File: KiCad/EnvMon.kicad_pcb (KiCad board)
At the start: 2 copper layers, 44.5 x 37 mm, 22 parts, among them J1 USB-C, J2 DC, J3 GPIO, M2 OLED1.5-RGB, M3 SCD30-4pin, U1 FT231XQ, U2 ESP32-WROOM-32

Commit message: Tidy
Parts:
- removed the R10 at (132.0, 91.5)
- added R3: 732R, RevK:R_0603, F.Cu at (99.2, 68.9)
- added R4: 2K, RevK:R_0603, F.Cu at (99.2, 66.5)
- added R5: 324R, RevK:R_0603, F.Cu at (99.2, 67.7)
- D1: value LED -> RGB; footprint LED_SMD:LED_0603_1608Metric -> RevK:LED-RGB-1.6x1.6
- J3: footprint Connector_Molex:Molex_SPOX_5268-08A_1x08_P2.50mm_Horizontal -> RevK:Molex_MiniSPOX_H8RA
- moved D1 43.3 mm to (99.2, 64.7), turned to 180 degrees
- moved J3 8.75 mm to (117.8, 93.2)
- renumbered Logo3 to Logo1, Logo1 to Logo2, Logo2 to Logo3, M3 to M1, R7 to R10, R8 to R11, R9 to R12, R3 to R6, R4 to R7, R5 to R8, R6 to R9
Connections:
- D1 pad 1: Net-(D1-Pad1) -> +3V3
- U2 pad 14: Net-(U2-Pad14) -> R
- U2 pad 23: Net-(U2-Pad23) -> B
- U2 pad 24: Net-(D1-Pad1) -> G
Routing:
- net GND: track 75.8 -> 145.3 mm, vias 1 -> 2
- net G: track 0.00 -> 46.6 mm, vias 0 -> 2
- net B: track 0.00 -> 43.8 mm, vias 0 -> 2
- net R: track 0.00 -> 40.0 mm, vias 0 -> 4
- net Net-(D1-Pad1): track 14.8 -> 0.00 mm, vias 2 -> 0
- net +3V3: track 104.9 -> 97.5 mm, vias 5 -> 4
- net Net-(U1-Pad1): track 48.1 -> 52.8 mm
- net Net-(D1-Pad2): track 1.52 -> 5.97 mm
- net Net-(D1-Pad4): track 0.00 -> 3.44 mm
- net IO4: track 25.8 -> 28.7 mm
- net IO3: track 33.2 -> 30.6 mm
- net Net-(U1-Pad18): track 30.3 -> 32.7 mm
- net IO1: track 21.9 -> 20.0 mm
- net Net-(U1-Pad19): track 55.9 -> 54.5 mm
- net IO2: track 20.4 -> 21.8 mm
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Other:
- board text added: "2021-07-20"
- board text removed: "2021-06-17"

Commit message: Move resistors
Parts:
- R1, R2: moved to F.Cu
- moved R1 8.76 mm to (93.3, 92.5)
- moved R2 7.91 mm to (91.8, 92.5)
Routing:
- net GND: track 145.3 -> 160.4 mm, vias 2 -> 3
- net Net-(J1-PadB5): track 9.14 -> 13.3 mm, vias 1 -> 2
- net Net-(J1-PadA5): track 11.8 -> 9.69 mm, vias 1 -> 2
- net IO6: track 29.2 -> 30.2 mm
- net Net-(J1-PadA7): track 7.92 -> 8.90 mm
- net Net-(J1-PadA6): track 8.06 -> 8.99 mm
- net Net-(J1-PadA4): track 31.8 -> 30.9 mm

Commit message: Library update
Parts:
- removed Reg1: Regulator, RevK:RegulatorBlock
- added C1: 0.1uF, RevK:Hidden, F.Cu at (95.3, 78.5)
- added C2: 2.2uF, RevK:Hidden, F.Cu at (96.5, 82.0)
- added C3: 10uF, RevK:Hidden, F.Cu at (102.8, 82.0)
- added D1: Schottky, RevK:Hidden, F.Cu at (99.7, 81.7)
- added L1: 6.8uH, RevK:Hidden, F.Cu at (101.3, 78.5)
- added U1: LMR16006YQ3, RevK:RegulatorBlock, F.Cu at (97.4, 78.5)
- renumbered D1 to D2, U1 to U2, U2 to U3

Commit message: Kicad 6
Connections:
- J1 pad A8: Net-(J1-PadA8) -> unconnected-(J1-PadA8)
- J1 pad B8: Net-(J1-PadB8) -> unconnected-(J1-PadB8)
- U2 pad 14: Net-(U2-Pad14) -> unconnected-(U2-Pad14)
- U2 pad 15: Net-(U2-Pad15) -> unconnected-(U2-Pad15)
- U2 pad 16: Net-(U2-Pad16) -> unconnected-(U2-Pad16)
- U2 pad 7: Net-(U2-Pad7) -> unconnected-(U2-Pad7)
- U3 pad 17: Net-(U3-Pad17) -> unconnected-(U3-Pad17)
- U3 pad 18: Net-(U3-Pad18) -> unconnected-(U3-Pad18)
- U3 pad 19: Net-(U3-Pad19) -> unconnected-(U3-Pad19)
- U3 pad 20: Net-(U3-Pad20) -> unconnected-(U3-Pad20)
- U3 pad 21: Net-(U3-Pad21) -> unconnected-(U3-Pad21)
- U3 pad 22: Net-(U3-Pad22) -> unconnected-(U3-Pad22)
- U3 pad 32: Net-(U3-Pad32) -> unconnected-(U3-Pad32)
- U3 pad 4: Net-(U3-Pad4) -> unconnected-(U3-Pad4)
- U3 pad 5: Net-(U3-Pad5) -> unconnected-(U3-Pad5)
- U3 pad 6: Net-(U3-Pad6) -> unconnected-(U3-Pad6)
- U3 pad 7: Net-(U3-Pad7) -> unconnected-(U3-Pad7)
- U3 pad 8: Net-(U3-Pad8) -> unconnected-(U3-Pad8)
- U3 pad 9: Net-(U3-Pad9) -> unconnected-(U3-Pad9)
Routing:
- net IO4: track 28.7 -> 27.8 mm
- net GND: track 160.4 -> 159.6 mm
- net OLED-MOSI: track 36.9 -> 36.1 mm
- net Net-(U2-Pad18): track 32.7 -> 32.1 mm
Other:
- net class Default removed

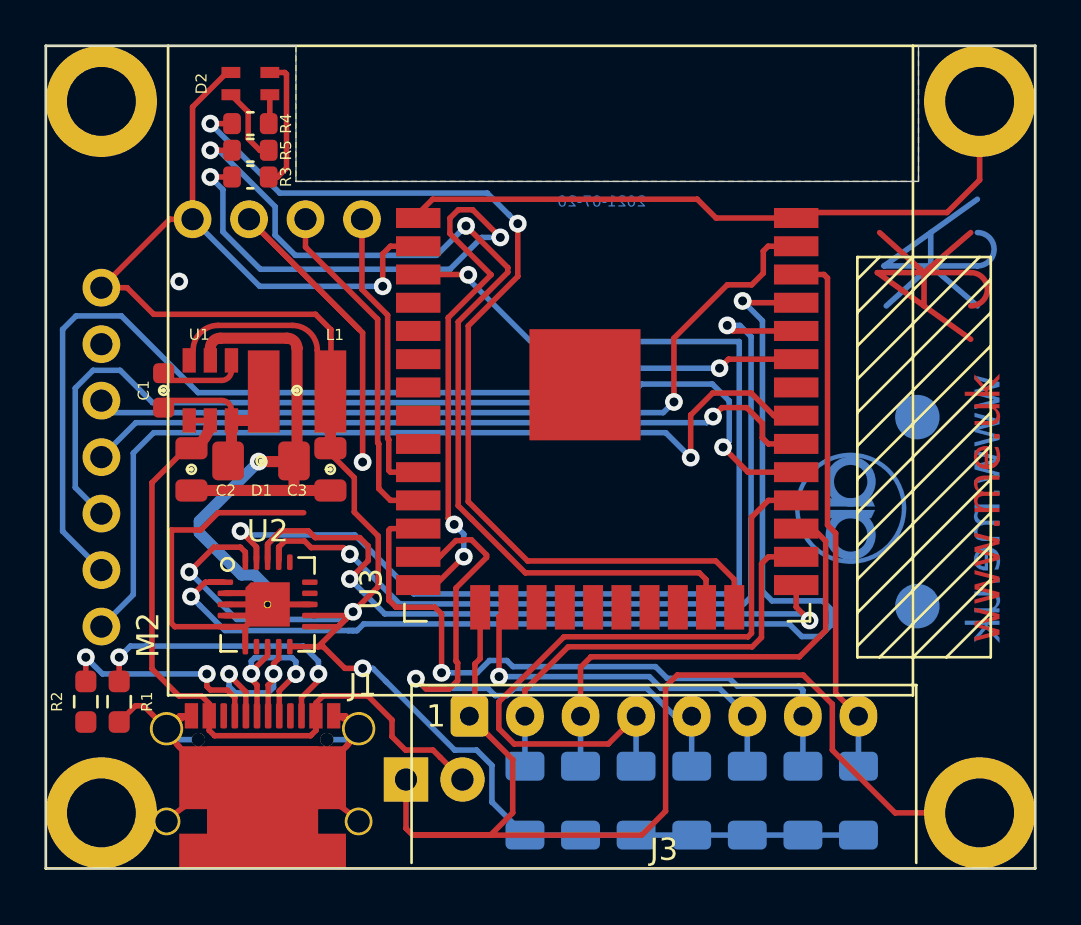
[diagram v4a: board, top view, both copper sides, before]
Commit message: More KiCad 6 tweaks
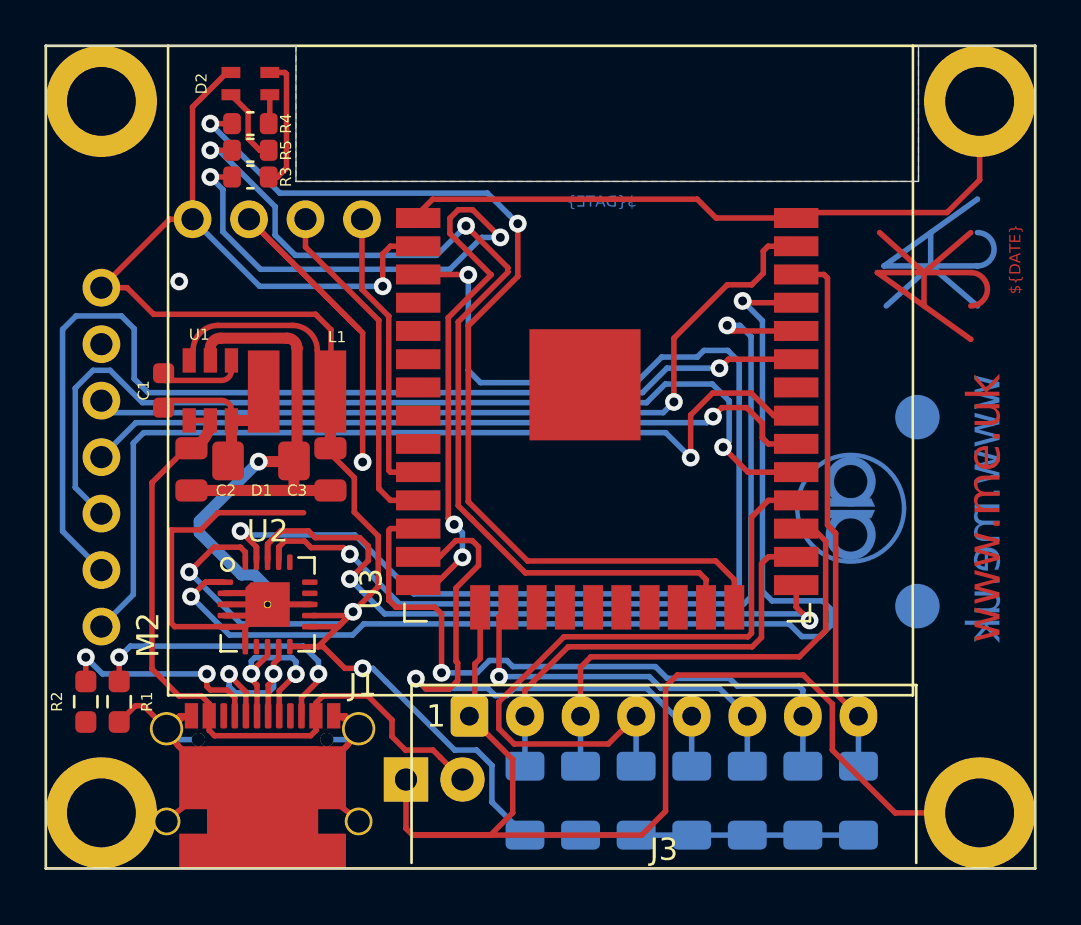
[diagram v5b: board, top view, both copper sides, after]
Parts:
- turned L1 to 180 degrees
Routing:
- net Net-(U2-Pad19): track 54.5 -> 56.0 mm
- net OLED-DC: track 46.8 -> 48.2 mm
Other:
- board text added: "${DATE}"
- board text removed: "2021-07-20"

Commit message: New PSU
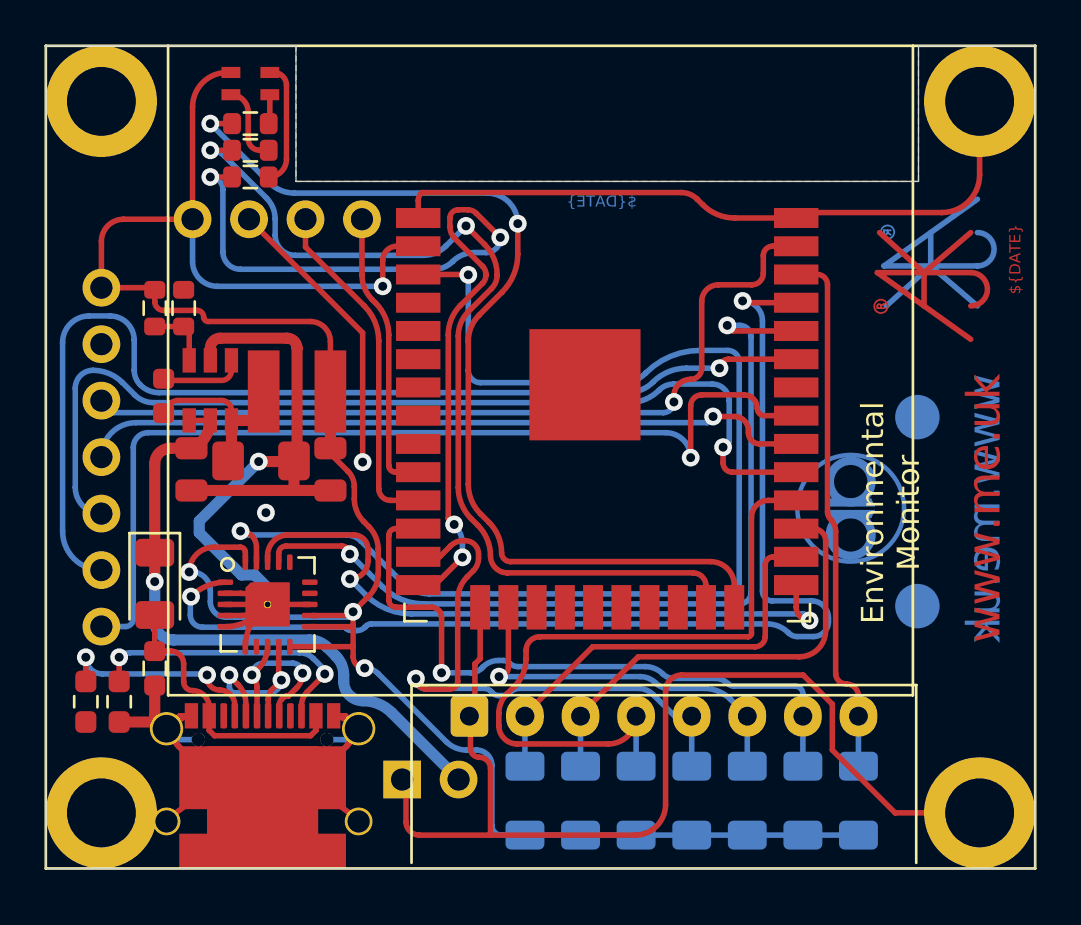
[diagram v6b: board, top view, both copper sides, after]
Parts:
- added C4: 10nF, RevK:C_0603, F.Cu at (94.9, 91.0)
- added D2: D, Diode_SMD:D_1206_3216Metric, F.Cu at (94.9, 87.2)
- added R1: 10M 1% or 0R, RevK:R_0603, F.Cu at (94.9, 74.8)
- added R2: 3M 1% or NF, RevK:R_0603, F.Cu at (96.2, 74.8)
- J2: footprint RevK:DC -> Connector_PinHeader_2.54mm:PinHeader_1x02_P2.54mm_Vertical
- U1: value LMR16006YQ3 -> LMR16006+FB; footprint RevK:RegulatorBlock -> RevK:RegulatorBlockFB
- moved C1 0.25 mm to (95.3, 78.8)
- moved J2 0.17 mm to (106.0, 96.0), turned to -90 degrees
- renumbered D2 to D3, R8 to R10, R9 to R11, R10 to R12, R11 to R13, R12 to R14, R1 to R3, R2 to R4, R3 to R5, R4 to R6, R5 to R7, R6 to R8, R7 to R9
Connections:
- J1 pad A4: Net-(J1-PadA4) -> VBUS
- J1 pad A9: Net-(J1-PadA4) -> VBUS
- J1 pad B4: Net-(J1-PadA4) -> VBUS
- J1 pad B9: Net-(J1-PadA4) -> VBUS
- J2 pad 2: Net-(J1-PadA4) -> DC
- U1 pad 1: Net-(J1-PadA4) -> DC
- U1 pad 2: Net-(J1-PadA4) -> DC
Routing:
- net Net-(J1-PadA4): track 30.9 -> 0.00 mm
- net GND: track 159.6 -> 128.8 mm
- net DC: track 0.00 -> 27.1 mm, vias 0 -> 1
- net VBUS: track 0.00 -> 12.5 mm
- net Net-(R1-Pad2): track 0.00 -> 2.96 mm
- net +3V3: track 97.6 -> 99.7 mm
- net G: track 46.6 -> 44.9 mm
- net Net-(U2-Pad18): track 32.1 -> 30.7 mm
- net OLED-MOSI: track 36.1 -> 37.4 mm
- net IO2: track 21.8 -> 20.7 mm
- net OLED-RST: track 42.1 -> 43.2 mm
- net Net-(U2-Pad17): track 40.1 -> 39.2 mm
- net IO3: track 30.6 -> 31.5 mm
- net Net-(U2-Pad19): track 56.0 -> 55.2 mm
- net Net-(J1-PadA7): track 8.90 -> 8.26 mm
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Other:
- board text added: "Environmental Monitor"

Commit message: Resitors
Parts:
- R1: value 10M 1% or 0R -> 100k 1% or 0R
- R2: value 3M 1% or NF -> 30k 1% or NF
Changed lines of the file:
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@@
       (primitives
     (gr_arc (start 2.89 -3.045) (mid 0 -0.155) (end -2.89 -3.045) (width 0.25))
-    (gr_arc (start 4.294753 -3.49127) (mid -0.016568 -1.026234) (end -4.311371 -3.519937) (width 0.25))
+    (gr_arc (start 4.294753 -3.49127) (mid -0.012228 -1.026222) (end -4.307036 -3.512417) (width 0.25))
     (gr_arc (start -3.2 -2.485) (mid -4.015 -3.3) (end -3.2 -4.115) (width 0.25))
     (gr_arc (start 3.2 -4.115) (mid 4.015 -3.3) (end 3.2 -2.485) (width 0.25))
@@
       (effects (font (size 0.5 0.5) (thickness 0.08)))
     )
-    (fp_text value "10M 1% or 0R" (at 0 0 90) (layer "F.Fab")
+    (fp_text value "100k 1% or 0R" (at 0 0 90) (layer "F.Fab")
       (effects (font (size 0.4 0.4) (thickness 0.08)))
     )
@@
       (effects (font (size 0.5 0.5) (thickness 0.08)))
     )
-    (fp_text value "3M 1% or NF" (at 0 0 90) (layer "F.Fab")
+    (fp_text value "30k 1% or NF" (at 0 0 90) (layer "F.Fab")
       (effects (font (size 0.4 0.4) (thickness 0.08)))
     )
